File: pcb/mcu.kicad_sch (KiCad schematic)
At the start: 1 part

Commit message: continued work on schematic
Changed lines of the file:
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@@
     (effects (font (size 1.27 1.27)) (justify left bottom))
+  )
+  (hierarchical_label "status" (shape output) (at 177.8 86.36 0) (fields_autoplaced)
+    (effects (font (size 1.27 1.27)) (justify left))
   )
   (hierarchical_label "CH5" (shape output) (at 177.8 104.14 0) (fields_autoplaced)

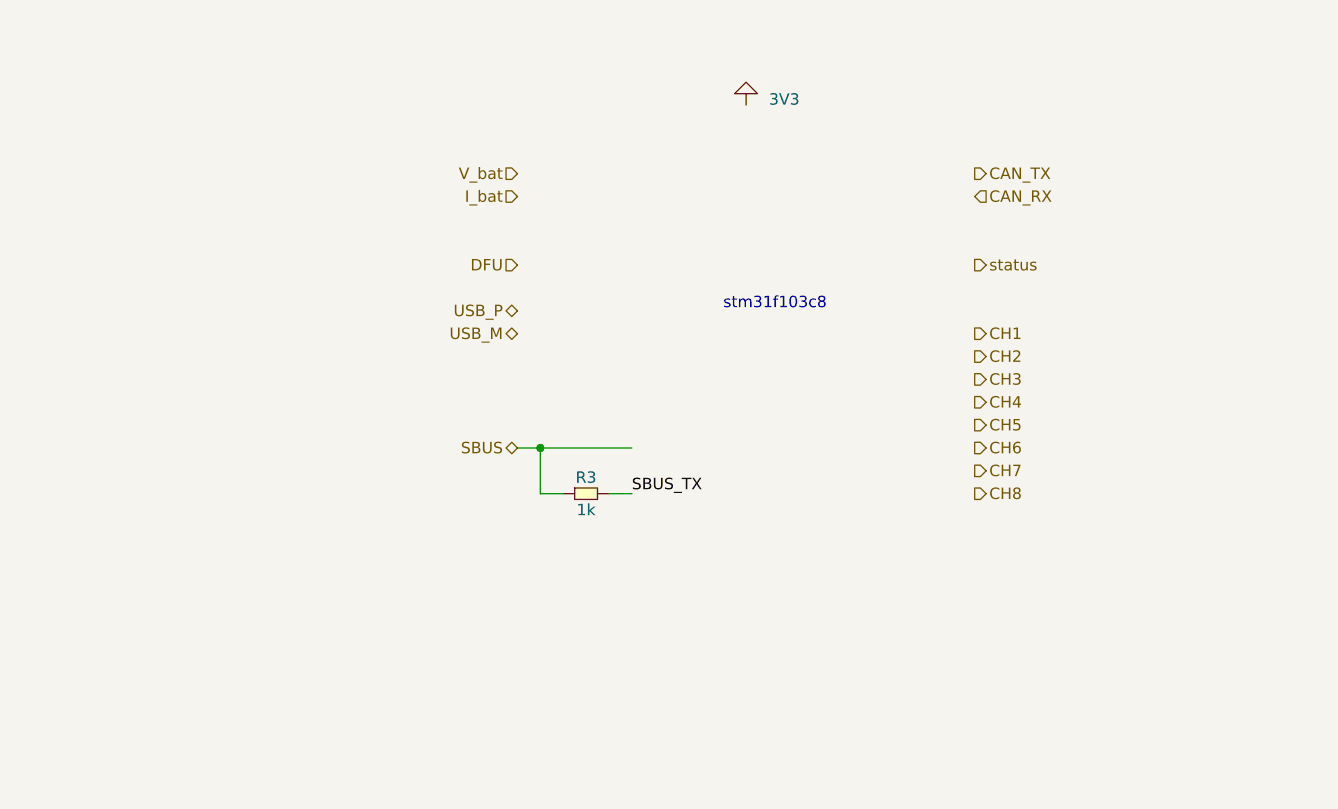
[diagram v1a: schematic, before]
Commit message: changed mcu layout to allow all desired features. added stm32 to schematic
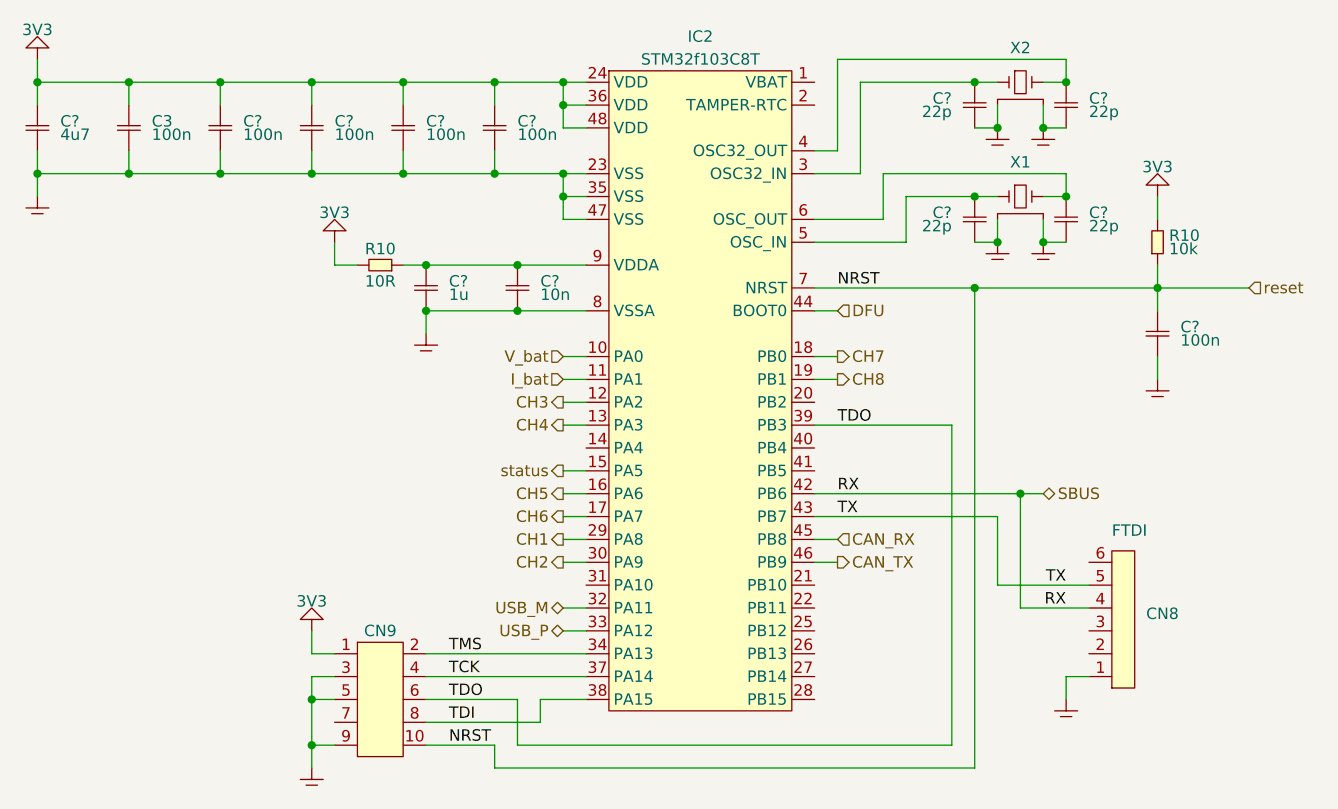
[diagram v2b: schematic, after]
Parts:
- removed R3: 1k, SMT:0603, symbol generic:R
- added C3, C? (x5): 100n, SMT:0603, symbol generic:C
- added C? (x4): 22p, SMT:0603, symbol generic:C
- added C?: 1u, SMT:0603, symbol generic:C
- added C?: 4u7, SMT:0603, symbol generic:C
- added C?: 10n, SMT:0603, symbol generic:C
- added CN8: 1x6, pin_headers:1x6, symbol pin_headers:1x6
- added CN9: 2x5, pin_headers:2x5, symbol pin_headers:2x5
- added IC2: STM32f103C8T, symbol MCU:STM32f103C8T
- added R10: 10k, SMT:0603, symbol generic:R
- added R10: 10R, SMT:0603, symbol generic:R
- added X1, X2: ~, symbol generic:xtal_gnd
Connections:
- net 3V3: now also C3.1, C?.1, C?.1, C?.1, C?.1, C?.1, CN9.1, IC2.24 (VDD), IC2.36 (VDD), IC2.48 (VDD), R10.2, R10.2
- net CAN_RX: now also IC2.45 (PB8)
- net CAN_TX: now also IC2.46 (PB9)
- net CH1: now also IC2.29 (PA8)
- net CH2: now also IC2.30 (PA9)
- net CH3: now also IC2.12 (PA2)
- net CH4: now also IC2.13 (PA3)
- net CH5: now also IC2.16 (PA6)
- net CH6: now also IC2.17 (PA7)
- net CH7: now also IC2.18 (PB0)
- net CH8: now also IC2.19 (PB1)
- net DFU: now also IC2.44 (BOOT0)
- net I_bat: now also IC2.11 (PA1)
- net SBUS: now also CN8.4, IC2.42 (PB6)
- net USB_M: now also IC2.32 (PA11)
- net USB_P: now also IC2.33 (PA12)
- net V_bat: now also IC2.10 (PA0)
- net status: now also IC2.15 (PA5)
- new net: C?.1, IC2.5 (OSC_IN), X1.1
- new net: C?.1, IC2.6 (OSC_OUT), X1.3
- new net: C?.1, IC2.3 (OSC32_IN), X2.1
- new net: C?.1, IC2.4 (OSC32_OUT), X2.3
- new net: C?.1, C?.1, IC2.9 (VDDA), R10.1
- new net GND: C3.2, C?.2, C?.2, C?.2, C?.2, C?.2, C?.2, C?.2, C?.2, C?.2, C?.2, C?.2, C?.2, CN8.1, CN9.3, CN9.5, CN9.9, IC2.23 (VSS), IC2.35 (VSS), IC2.47 (VSS), IC2.8 (VSSA), X1.2, X1.4, X2.2, X2.4
- new net TCK: CN9.4, IC2.37 (PA14)
- new net TDI: CN9.8, IC2.38 (PA15)
- new net TDO: CN9.6, IC2.39 (PB3)
- new net TMS: CN9.2, IC2.34 (PA13)
- new net TX: CN8.5, IC2.43 (PB7)
- new net reset: C?.1, CN9.10, IC2.7 (NRST), R10.1
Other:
- note added: "FTDI"
- note removed: "stm31f103c8"

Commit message: schematic mostly done
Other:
- title: (none) -> CAN bus to RC servo adapter
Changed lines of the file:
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@@
 (kicad_sch (version 20230121) (generator eeschema)
   (paper "A4")
+  (title_block
+    (title "CAN bus to RC servo adapter")
+    (date "2024-01-10")
+    (rev "0")
+    (comment 1 "Microcontroller and programming headers")
+  )
   (junction (at 187.96 66.04) (diameter 0) (color 0 0 0 0)
   )

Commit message: started work on layout
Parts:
- added TP1, TP10, TP11, TP2, TP3, TP4, TP5, TP6, TP7, TP8, TP9: test_point, PCB:test_point, symbol PCB:test_point
- IC2: footprint (none) -> QFP:LQFP-48
- renumbered CN8 to CN11
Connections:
- net at IC2.14 (PA4): now also TP1.1 (TP)
- net at IC2.20 (PB2): now also TP3.1 (TP)
- net at IC2.21 (PB10): now also TP6.1 (TP)
- net at IC2.22 (PB11): now also TP7.1 (TP)
- net at IC2.25 (PB12): now also TP8.1 (TP)
- net at IC2.26 (PB13): now also TP9.1 (TP)
- net at IC2.27 (PB14): now also TP10.1 (TP)
- net at IC2.28 (PB15): now also TP11.1 (TP)
- net at IC2.31 (PA10): now also TP2.1 (TP)
- net at IC2.40 (PB4): now also TP4.1 (TP)
- net at IC2.41 (PB5): now also TP5.1 (TP)

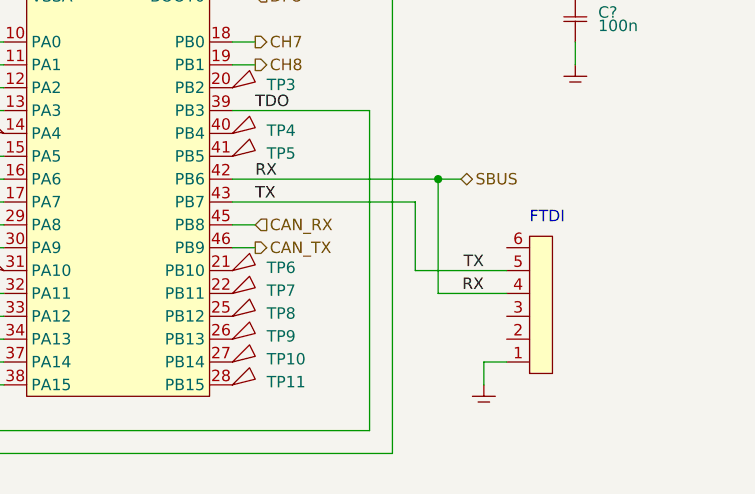
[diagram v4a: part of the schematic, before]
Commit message: removed FTDI and SBUS headers for now
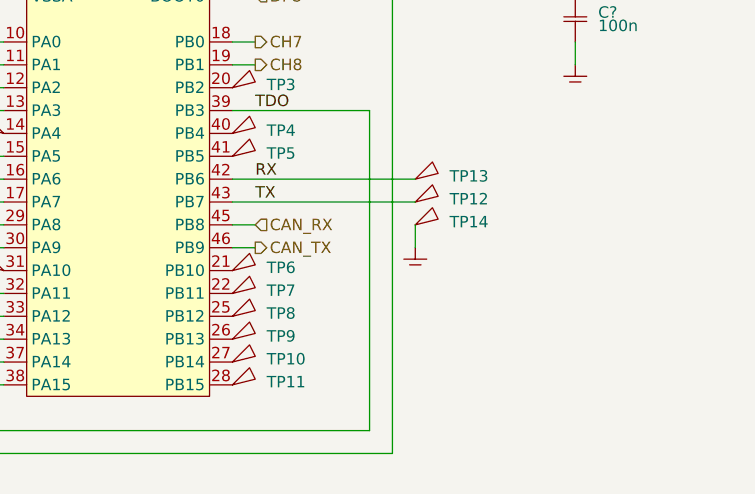
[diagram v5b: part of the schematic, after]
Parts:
- removed CN11: 1x6, pin_headers:1x6, symbol pin_headers:1x6
- added TP12, TP13, TP14: test_point, PCB:test_point, symbol PCB:test_point
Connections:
- net GND: now also TP14.1 (TP)
- net TX: now also TP12.1 (TP)
- net SBUS renamed RX
- net RX: now also TP13.1 (TP)
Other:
- note removed: "FTDI"
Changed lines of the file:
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@@
   (junction (at 132.08 68.58) (diameter 0) (color 0 0 0 0)
   )
-  (junction (at 182.88 111.76) (diameter 0) (color 0 0 0 0)
-  )
   (junction (at 104.14 134.62) (diameter 0) (color 0 0 0 0)
   )
@@
     (stroke (width 0) (type default))
   )
-  (wire (pts (xy 182.88 124.46) (xy 182.88 111.76))
-    (stroke (width 0) (type default))
-  )
-  (wire (pts (xy 180.34 121.92) (xy 190.5 121.92))
-    (stroke (width 0) (type default))
-  )
   (wire (pts (xy 132.08 127) (xy 134.62 127))
     (stroke (width 0) (type default))
@@
     (stroke (width 0) (type default))
   )
-  (wire (pts (xy 182.88 124.46) (xy 190.5 124.46))
-    (stroke (width 0) (type default))
-  )
   (wire (pts (xy 104.14 129.54) (xy 106.68 129.54))
     (stroke (width 0) (type default))
@@
     (stroke (width 0) (type default))
   )
-  (wire (pts (xy 160.02 111.76) (xy 182.88 111.76))
+  (wire (pts (xy 160.02 111.76) (xy 180.34 111.76))
     (stroke (width 0) (type default))
   )
@@
     (stroke (width 0) (type default))
   )
+  (wire (pts (xy 180.34 116.84) (xy 180.34 119.38))
+    (stroke (width 0) (type default))
+  )
   (wire (pts (xy 132.08 96.52) (xy 134.62 96.52))
     (stroke (width 0) (type default))
@@
     (stroke (width 0) (type default))
   )
-  (wire (pts (xy 187.96 132.08) (xy 187.96 134.62))
-    (stroke (width 0) (type default))
-  )
   (wire (pts (xy 177.8 78.74) (xy 180.34 78.74))
     (stroke (width 0) (type default))
@@
     (stroke (width 0) (type default))
   )
-  (wire (pts (xy 190.5 132.08) (xy 187.96 132.08))
-    (stroke (width 0) (type default))
-  )
   (wire (pts (xy 132.08 71.12) (xy 132.08 68.58))
     (stroke (width 0) (type default))
@@
     (stroke (width 0) (type default))
   )
-  (wire (pts (xy 180.34 114.3) (xy 180.34 121.92))
-    (stroke (width 0) (type default))
-  )
   (wire (pts (xy 124.46 139.7) (xy 124.46 142.24))
     (stroke (width 0) (type default))
@@
     (stroke (width 0) (type default))
   )
-  (wire (pts (xy 182.88 111.76) (xy 185.42 111.76))
-    (stroke (width 0) (type default))
-  )
   (wire (pts (xy 106.68 86.36) (xy 109.22 86.36))
     (stroke (width 0) (type default))
@@
   (wire (pts (xy 185.42 66.04) (xy 187.96 66.04))
     (stroke (width 0) (type default))
-  )
-  (text "FTDI" (at 193.04 116.84 0)
-    (effects (font (size 1.27 1.27)) (justify left bottom))
-  )
-  (label "TX" (at 187.96 121.92 180) (fields_autoplaced)
-    (effects (font (size 1.27 1.27)) (justify right bottom))
   )
   (label "TMS" (at 119.38 129.54 0) (fields_autoplaced)
@@
     (effects (font (size 1.27 1.27)) (justify left bottom))
   )
-  (label "RX" (at 187.96 124.46 180) (fields_autoplaced)
-    (effects (font (size 1.27 1.27)) (justify right bottom))
-  )
   (label "TDI" (at 119.38 137.16 0) (fields_autoplaced)
     (effects (font (size 1.27 1.27)) (justify left bottom))
@@
     (effects (font (size 1.27 1.27)) (justify right))
   )
-  (hierarchical_label "SBUS" (shape bidirectional) (at 185.42 111.76 0) (fields_autoplaced)
-    (effects (font (size 1.27 1.27)) (justify left))
-  )
   (hierarchical_label "CH6" (shape output) (at 132.08 114.3 180) (fields_autoplaced)
     (effects (font (size 1.27 1.27)) (justify right))
@@
         (path "/6bb3bad6-1a89-4624-b34d-6ddda7dd16d2/19469851-aeaf-466c-9786-c0d0ae531cf4"
           (reference "C16") (unit 1)
+        )
+      )
+    )
+  )
+  (symbol (lib_id "generic:GND") (at 180.34 119.38 0) (unit 1)
+    (in_bom yes) (on_board yes) (dnp no) (fields_autoplaced)
+    (property "Reference" "#GND020" (at 184.15 118.11 0)
+      (effects (font (size 1.27 1.27)) hide)
+    )
+    (property "Value" "GND" (at 184.15 119.38 0)
+      (effects (font (size 1.27 1.27)) hide)
+    )
+    (property "Footprint" "" (at 180.34 119.38 0)
+      (effects (font (size 1.27 1.27)) hide)
+    )
+    (property "Datasheet" "" (at 180.34 119.38 0)
+      (effects (font (size 1.27 1.27)) hide)
+    )
+    (pin "~")
+    (instances
+      (project "pcb"
+        (path "/6bb3bad6-1a89-4624-b34d-6ddda7dd16d2/19469851-aeaf-466c-9786-c0d0ae531cf4"
+          (reference "#GND020") (unit 1)
         )
       )
@@
     )
   )
+  (symbol (lib_id "PCB:test_point") (at 180.34 116.84 0) (unit 1)
+    (in_bom yes) (on_board yes) (dnp no) (fields_autoplaced)
+    (property "Reference" "TP14" (at 184.15 116.5225 0)
+      (effects (font (size 1.27 1.27)) (justify left))
+    )
+    (property "Value" "test_point" (at 180.34 114.3 0)
+      (effects (font (size 1.27 1.27)) hide)
+    )
+    (property "Footprint" "PCB:test_point" (at 182.88 118.11 0)
+      (effects (font (size 1.27 1.27)) hide)
+    )
+    (property "Datasheet" "" (at 180.34 116.84 0)
+      (effects (font (size 1.27 1.27)) hide)
+    )
+    (pin "1")
+    (instances
+      (project "pcb"
+        (path "/6bb3bad6-1a89-4624-b34d-6ddda7dd16d2/19469851-aeaf-466c-9786-c0d0ae531cf4"
+          (reference "TP14") (unit 1)
+        )
+      )
+    )
+  )
   (symbol (lib_id "PCB:test_point") (at 160.02 132.08 0) (unit 1)
     (in_bom yes) (on_board yes) (dnp no) (fields_autoplaced)
@@
     )
   )
-  (symbol (lib_id "pin_headers:1x6") (at 190.5 127 0) (mirror x) (unit 1)
-    (in_bom yes) (on_board yes) (dnp no)
-    (property "Reference" "CN11" (at 196.85 125.095 0)
-      (effects (font (size 1.27 1.27)) (justify left) hide)
-    )
-    (property "Value" "1x6" (at 190.5 134.62 0)
-      (effects (font (size 1.27 1.27)) hide)
-    )
-    (property "Footprint" "pin_headers:1x6" (at 190.5 132.08 0)
-      (effects (font (size 1.27 1.27)) hide)
-    )
-    (property "Datasheet" "" (at 190.5 127 0)
-      (effects (font (size 1.27 1.27)) hide)
-    )
-    (pin "1")
-    (pin "2")
-    (pin "3")
-    (pin "4")
-    (pin "5")
-    (pin "6")
-    (instances
-      (project "pcb"
-        (path "/6bb3bad6-1a89-4624-b34d-6ddda7dd16d2/19469851-aeaf-466c-9786-c0d0ae531cf4"
-          (reference "CN11") (unit 1)
-        )
-      )
-    )
-  )
   (symbol (lib_id "PCB:test_point") (at 160.02 134.62 0) (unit 1)
     (in_bom yes) (on_board yes) (dnp no) (fields_autoplaced)
@@
     )
   )
-  (symbol (lib_id "generic:GND") (at 187.96 134.62 0) (unit 1)
-    (in_bom yes) (on_board yes) (dnp no) (fields_autoplaced)
-    (property "Reference" "#GND020" (at 191.77 133.35 0)
-      (effects (font (size 1.27 1.27)) hide)
-    )
-    (property "Value" "GND" (at 191.77 134.62 0)
-      (effects (font (size 1.27 1.27)) hide)
-    )
-    (property "Footprint" "" (at 187.96 134.62 0)
-      (effects (font (size 1.27 1.27)) hide)
-    )
-    (property "Datasheet" "" (at 187.96 134.62 0)
-      (effects (font (size 1.27 1.27)) hide)
-    )
-    (pin "~")
-    (instances
-      (project "pcb"
-        (path "/6bb3bad6-1a89-4624-b34d-6ddda7dd16d2/19469851-aeaf-466c-9786-c0d0ae531cf4"
-          (reference "#GND020") (unit 1)
+  (symbol (lib_id "PCB:test_point") (at 180.34 114.3 0) (unit 1)
+    (in_bom yes) (on_board yes) (dnp no) (fields_autoplaced)
+    (property "Reference" "TP12" (at 184.15 113.9825 0)
+      (effects (font (size 1.27 1.27)) (justify left))
+    )
+    (property "Value" "test_point" (at 180.34 111.76 0)
+      (effects (font (size 1.27 1.27)) hide)
+    )
+    (property "Footprint" "PCB:test_point" (at 182.88 115.57 0)
+      (effects (font (size 1.27 1.27)) hide)
+    )
+    (property "Datasheet" "" (at 180.34 114.3 0)
+      (effects (font (size 1.27 1.27)) hide)
+    )
+    (pin "1")
+    (instances
+      (project "pcb"
+        (path "/6bb3bad6-1a89-4624-b34d-6ddda7dd16d2/19469851-aeaf-466c-9786-c0d0ae531cf4"
+          (reference "TP12") (unit 1)
         )
       )
@@
         )
       )
+    )
+  )
+  (symbol (lib_id "PCB:test_point") (at 180.34 111.76 0) (unit 1)
+    (in_bom yes) (on_board yes) (dnp no) (fields_autoplaced)
+    (property "Reference" "TP13" (at 184.15 111.4425 0)
+      (effects (font (size 1.27 1.27)) (justify left))
+    )
+    (property "Value" "test_point" (at 180.34 109.22 0)
+      (effects (font (size 1.27 1.27)) hide)
+    )
+    (property "Footprint" "PCB:test_point" (at 182.88 113.03 0)
+      (effects (font (size 1.27 1.27)) hide)
+    )
+    (property "Datasheet" "" (at 180.34 111.76 0)
+      (effects (font (size 1.27 1.27)) hide)
+    )
+    (pin "1")
+    (instances
+      (project "pcb"
+        (path "/6bb3bad6-1a89-4624-b34d-6ddda7dd16d2/19469851-aeaf-466c-9786-c0d0ae531cf4"
+          (reference "TP13") (unit 1)
+        )
+      )
